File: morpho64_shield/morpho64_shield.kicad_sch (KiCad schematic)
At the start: 7 parts, among them J1 CN7, J2 CN10, SW1 SW_DIP_x08

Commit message: esd + caps
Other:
- note added: "ADC2 signal goes to both internal ADC1CH2 and ADC2CH1 for flexibility"
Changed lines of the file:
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@@
 	(generator_version "10.0")
 	(paper "A4")
+	(text "ADC2 signal goes to both\ninternal ADC1CH2 and ADC2CH1\nfor flexibility\n\n"
+		(exclude_from_sim no)
+		(at 92.202 97.028 0)
+		(effects
+			(font
+				(size 1.27 1.27)
+			)
+		)
+	)
 	(junction
 		(at 55.88 148.59)

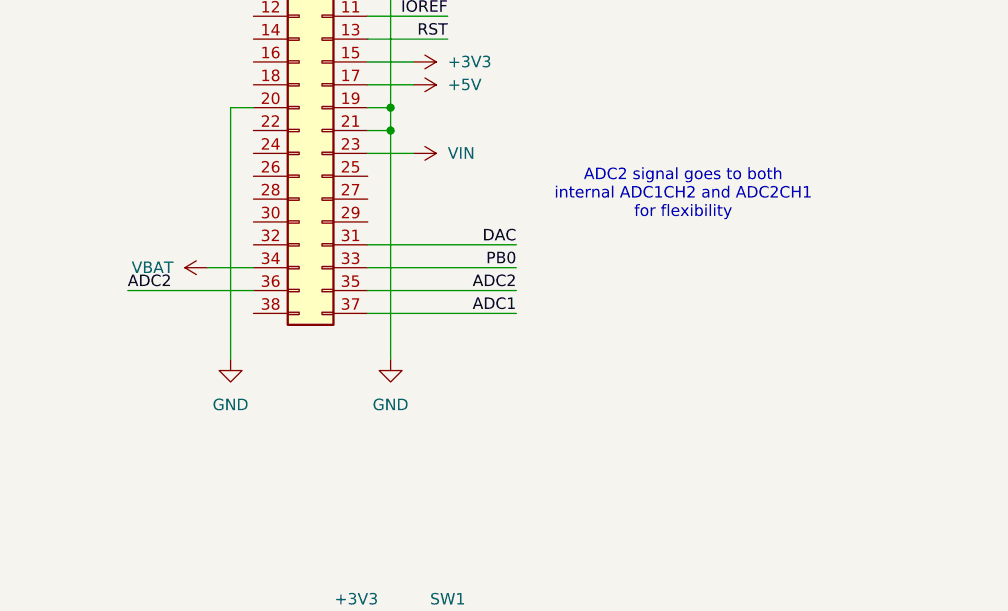
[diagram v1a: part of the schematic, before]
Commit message: First part of layout
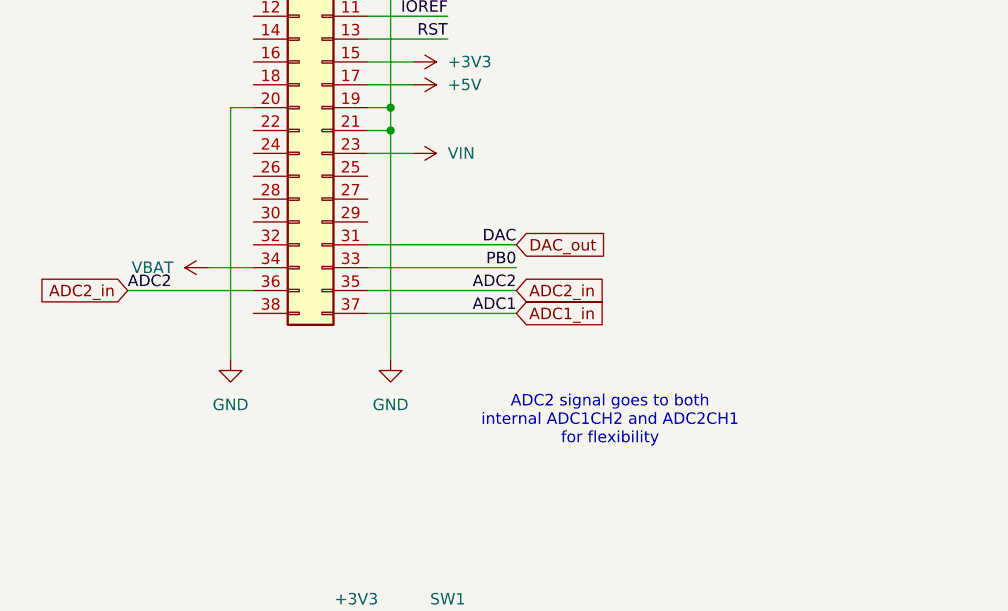
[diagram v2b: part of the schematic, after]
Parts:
- SW1: footprint (none) -> Button_Switch_SMD:SW_DIP_SPSTx08_Slide_Copal_CHS-08A_W5.08mm_P1.27mm_JPin
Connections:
- net ADC1 renamed ADC1_in
- net ADC2 renamed ADC2_in
- net DAC renamed DAC_out

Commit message: First PCB order
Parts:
- added R16: R, Resistor_SMD:R_0603_1608Metric, symbol Device:R
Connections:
- net +3V3: now also R16.1; no longer SW1.1, SW1.2, SW1.3, SW1.4, SW1.5, SW1.6, SW1.7, SW1.8
- new net: R16.2, SW1.1, SW1.2, SW1.3, SW1.4, SW1.5, SW1.6, SW1.7, SW1.8
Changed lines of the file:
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@@
 	(wire
 		(pts
+			(xy 55.88 140.97) (xy 55.88 148.59)
+		)
+		(stroke
+			(width 0)
+			(type default)
+		)
+	)
+	(wire
+		(pts
 			(xy 57.15 101.6) (xy 73.66 101.6)
 		)
@@
 	(wire
 		(pts
-			(xy 55.88 146.05) (xy 55.88 148.59)
+			(xy 55.88 129.54) (xy 55.88 133.35)
 		)
 		(stroke
@@
 	(symbol
 		(lib_id "power:+3V3")
-		(at 55.88 146.05 0)
+		(at 55.88 129.54 0)
 		(unit 1)
 		(body_style 1)
@@
 		(fields_autoplaced yes)
 		(property "Reference" "#PWR06"
-			(at 55.88 149.86 0)
+			(at 55.88 133.35 0)
 			(hide yes)
 			(show_name no)
@@
 		)
 		(property "Value" "+3V3"
-			(at 55.88 140.97 0)
+			(at 55.88 124.46 0)
 			(show_name no)
 			(do_not_autoplace no)
@@
 		)
 		(property "Footprint" ""
-			(at 55.88 146.05 0)
+			(at 55.88 129.54 0)
 			(hide yes)
 			(show_name no)
@@
 		)
 		(property "Datasheet" ""
-			(at 55.88 146.05 0)
+			(at 55.88 129.54 0)
 			(hide yes)
 			(show_name no)
@@
 		)
 		(property "Description" "Power symbol creates a global label with name \"+3V3\""
-			(at 55.88 146.05 0)
+			(at 55.88 129.54 0)
 			(hide yes)
 			(show_name no)
@@
 					(unit 1)
 				)
+			)
+		)
+	)
+	(symbol
+		(lib_id "Device:R")
+		(at 55.88 137.16 0)
+		(unit 1)
+		(body_style 1)
+		(exclude_from_sim no)
+		(in_bom yes)
+		(on_board yes)
+		(in_pos_files yes)
+		(dnp no)
+		(fields_autoplaced yes)
+		(property "Reference" "R16"
+			(at 58.42 135.8899 0)
+			(show_name no)
+			(do_not_autoplace no)
+			(effects
+				(font
+					(size 1.27 1.27)
+				)
+				(justify left)
+			)
+		)
+		(property "Value" "R"
+			(at 58.42 138.4299 0)
+			(show_name no)
+			(do_not_autoplace no)
+			(effects
+				(font
+					(size 1.27 1.27)
+				)
+				(justify left)
+			)
+		)
+		(property "Footprint" "Resistor_SMD:R_0603_1608Metric"
+			(at 54.102 137.16 90)
+			(hide yes)
+			(show_name no)
+			(do_not_autoplace no)
+			(effects
+				(font
+					(size 1.27 1.27)
+				)
+			)
+		)
+		(property "Datasheet" ""
+			(at 55.88 137.16 0)
+			(hide yes)
+			(show_name no)
+			(do_not_autoplace no)
+			(effects
+				(font
+					(size 1.27 1.27)
+				)
+			)
+		)
+		(property "Description" "Resistor"
+			(at 55.88 137.16 0)
+			(hide yes)
+			(show_name no)
+			(do_not_autoplace no)
+			(effects
+				(font
+					(size 1.27 1.27)
+				)
+			)
+		)
+		(pin "2"
+		)
+		(pin "1"
+		)
+		(instances
+			(project "morpho64_shield"
+				(path "/9278c48a-e3d9-46fc-9342-1a833157c1d8"
+					(reference "R16")
+					(unit 1)
+				)
